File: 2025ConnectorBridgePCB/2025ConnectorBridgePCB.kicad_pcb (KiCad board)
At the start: 2 copper layers, 95.5 x 80.5 mm, 10 parts, among them J1 SM03B-GHS-TBLFSN, J10 L77SDA15SA4CH4F, J11 L77SDA15SA4CH4F, J12 SM03B-GHS-TBLFSN, J2 SM03B-GHS-TBLFSN, J4 640389-5, J5 Screw_Terminal_01x08, J6 640389-5, J7 Screw_Terminal_01x08, J8 Conn_01x03_Socket

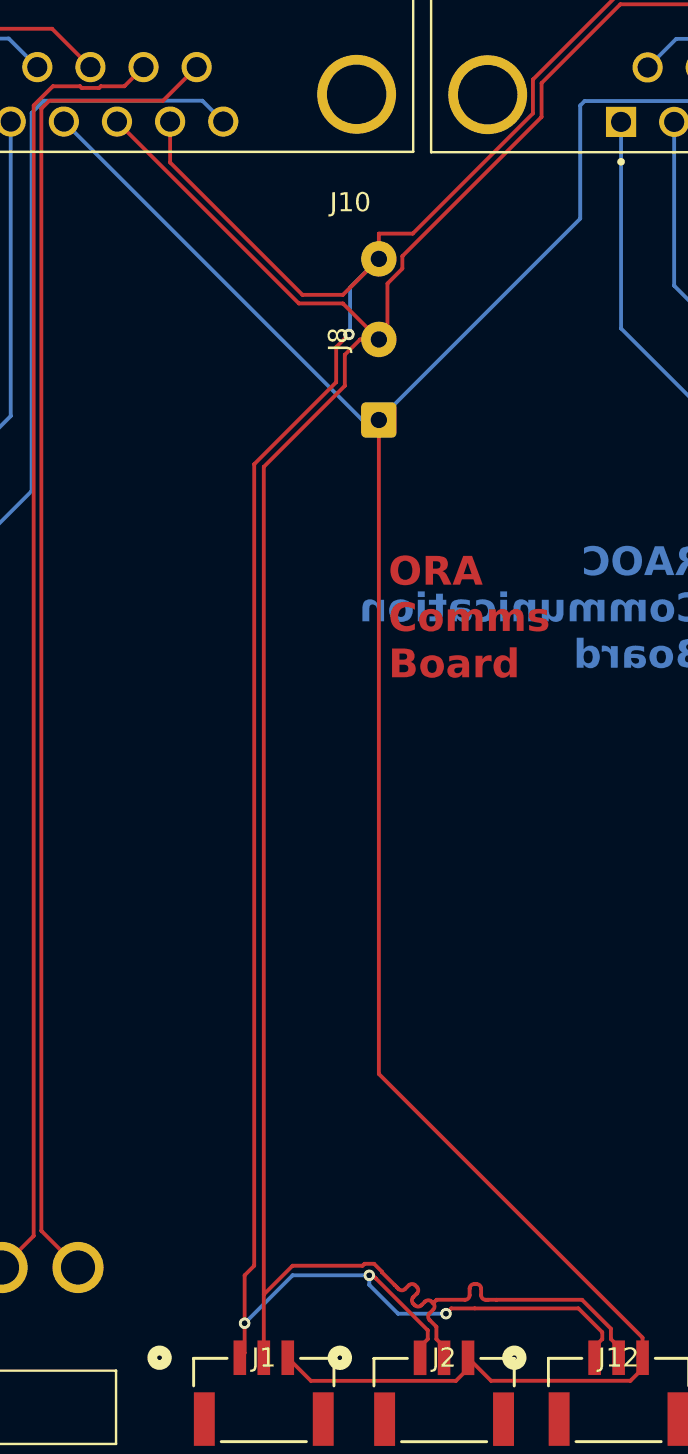
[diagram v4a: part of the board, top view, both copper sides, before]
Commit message: Comm Board: Push Latest Changes
Moved text back onto board, updated some traces.
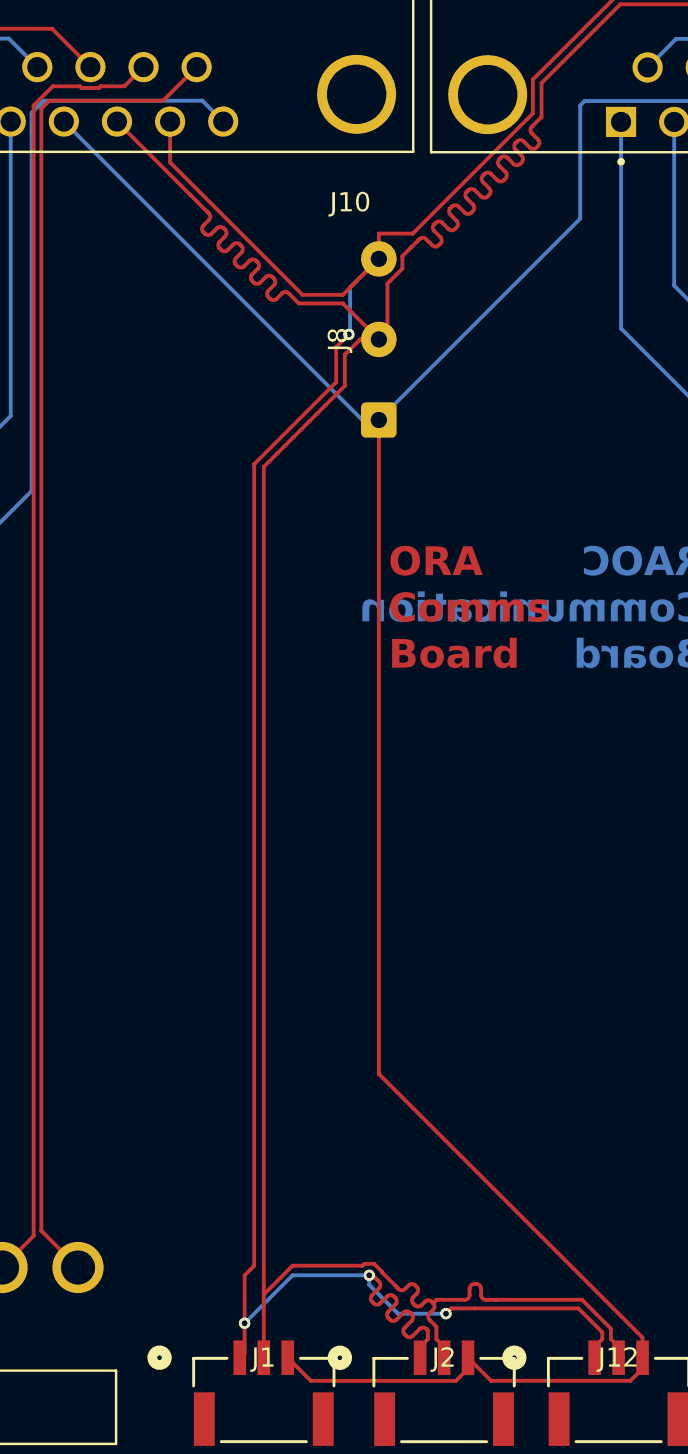
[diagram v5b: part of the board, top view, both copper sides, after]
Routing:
- net CAN-: track 144.3 -> 160.9 mm
- net CAN+: track 150.0 -> 154.6 mm

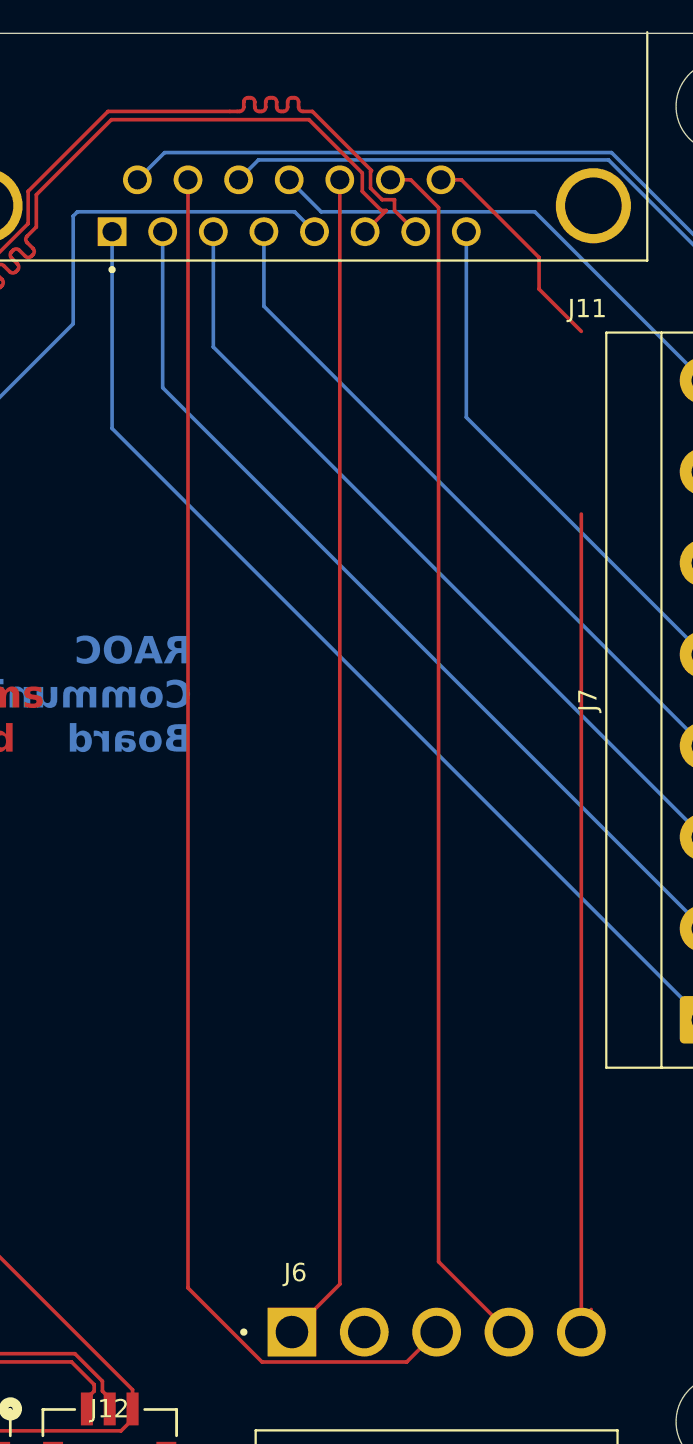
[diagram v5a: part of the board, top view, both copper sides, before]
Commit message: Comm Board: Fix MOT_B_ENCB and CAN line
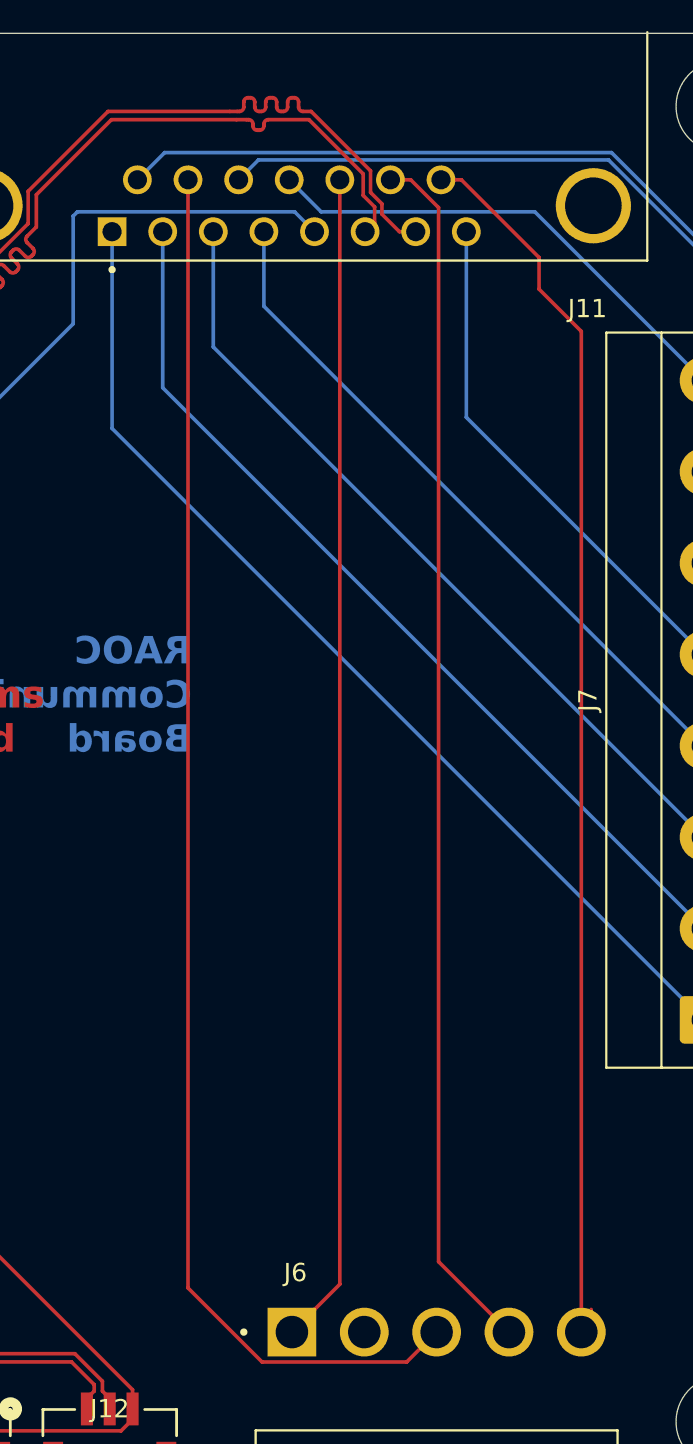
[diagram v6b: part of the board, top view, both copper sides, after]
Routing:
- net MOT_B_ENCB: track 57.6 -> 67.6 mm

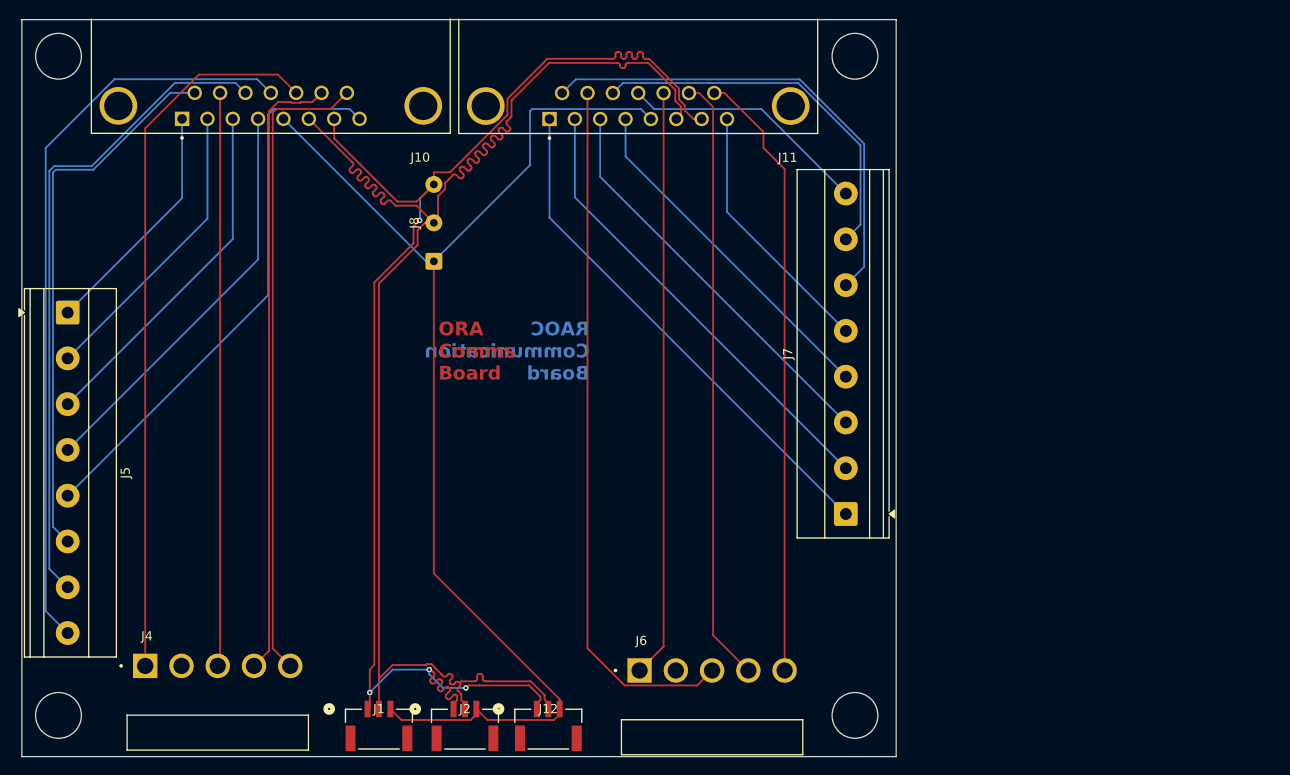
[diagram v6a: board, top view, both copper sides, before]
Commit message: Comm Board: Add changes from George
Added Ground Plane and moved text to silkscreen. Added ORA logo to silkscreen as well.
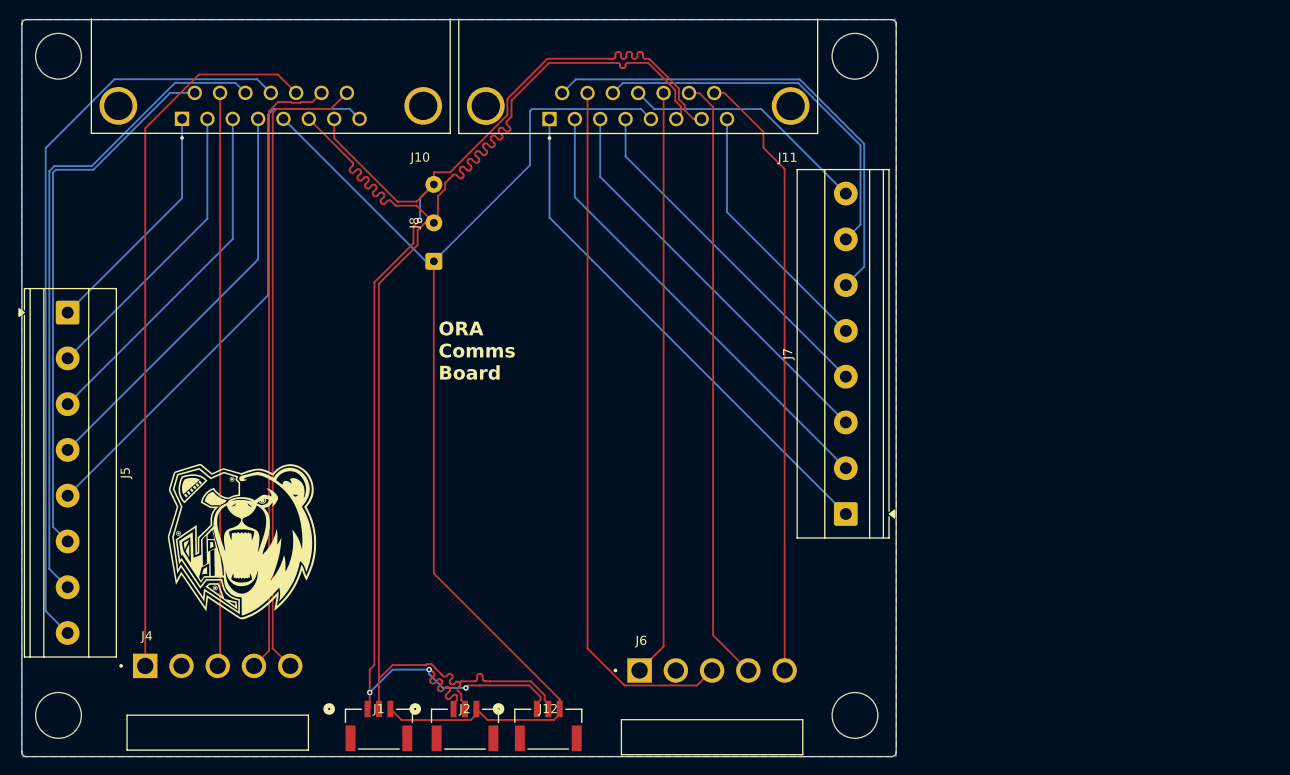
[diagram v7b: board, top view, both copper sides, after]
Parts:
- added G***: LOGO, ORA_Logo:ORA_Logo, F.Cu at (90.5, 112.0)
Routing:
- added copper zone on B.Cu, net GND
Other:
- outline, holes or cut-outs redrawn
- board text added: "Communication Board"
- board text removed: "RAOC Communication Board"
